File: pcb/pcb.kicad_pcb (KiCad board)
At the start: 6 copper layers, 243.4 x 148.8 mm, 178 parts, among them J1201 Conn_02x07_Top_Bottom, J1401 FPGA_JTAG, J201 USB_B_Mini, J301 Conn_02x07_Odd_Even, J302 1658525-9, J601 DB15_Female_HighDensity, J801 10067847-001RLF, J901 FTSH-110-01-L-DV-007, U1402 S25FL127SABMFV101, U201 TPS54325PWPR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

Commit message: fix new vga
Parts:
- J601: value DB15_Female_HighDensity -> AHDF15A-KG-TAXB; footprint vga:618015330923 -> assvga:AHDF15A-KG-TAXB
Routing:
- net GND: track 239.2 -> 245.0 mm, vias 151 -> 153
- net Net-(J601-Pad14): track 27.9 -> 29.2 mm
- net Net-(J601-Pad13): track 34.1 -> 35.1 mm
- net mcu_debug_reset: track 108.9 -> 109.5 mm
- net Net-(J601-Pad3): track 30.9 -> 31.4 mm

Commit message: logo
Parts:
- added G***: LOGO, raycraft:raycraft, F.Cu at (87.6, 114.8)
- moved J201 16.8 mm to (65.3, 35.4)
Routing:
- net Net-(C216-Pad1): track 56.7 -> 43.8 mm, vias 18 -> 2
- net GND: track 245.0 -> 257.9 mm, vias 153 -> 181
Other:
- board text added: "Carl Aarrestad Ole Peder Brandtzæg Emma Lu Eikemo Sindre Engøy Odd-Erik Frantzen Børge Lundsaunet Sivert Olstad Kasper Midttun Søreide"

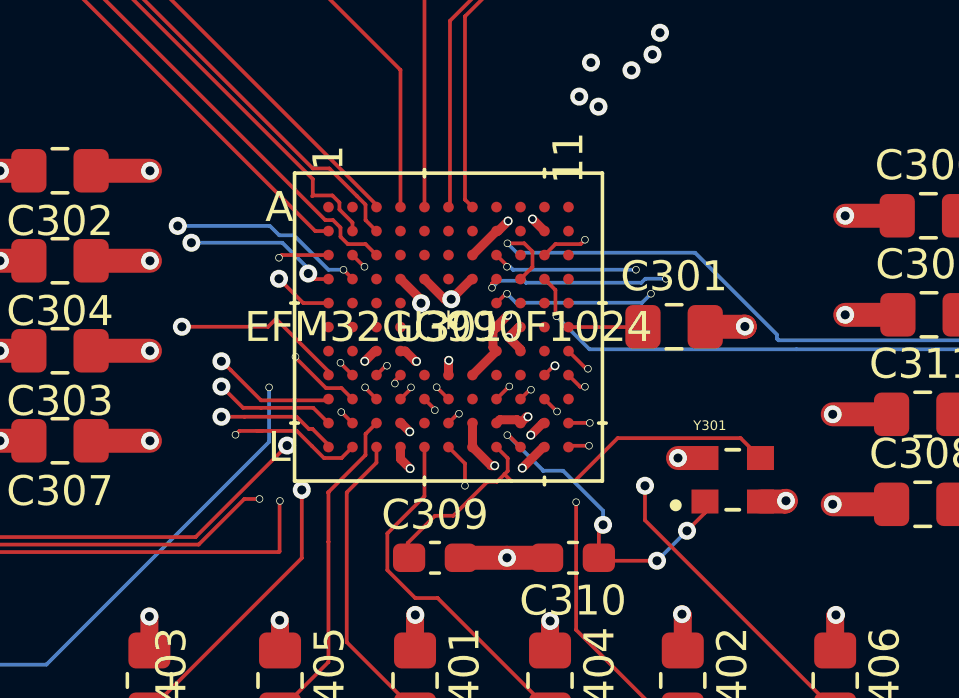
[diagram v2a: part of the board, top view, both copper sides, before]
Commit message: up via size, going to remove onboard-controller
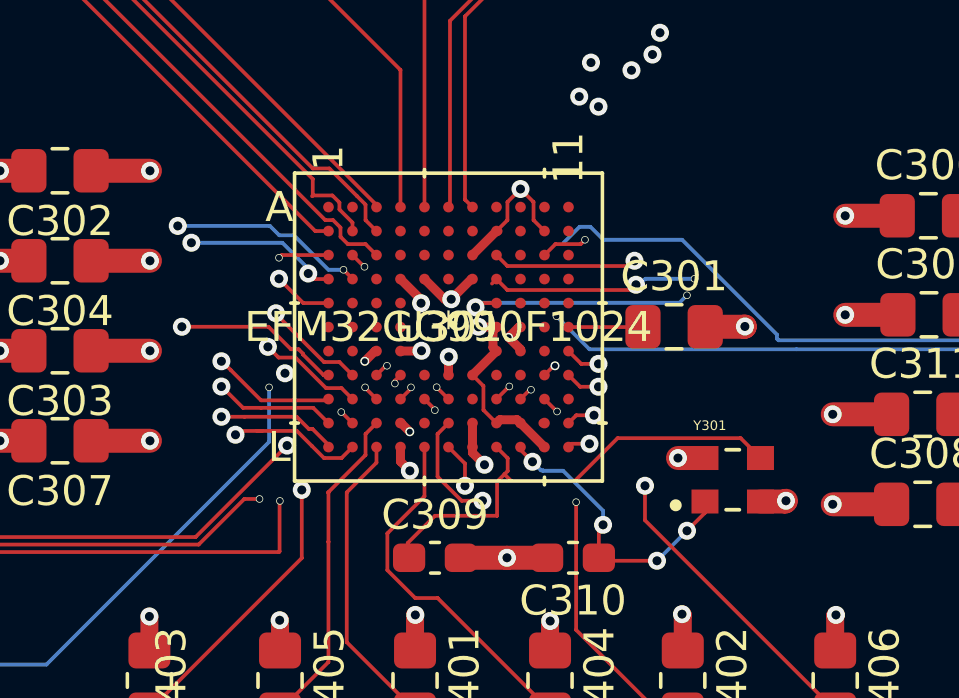
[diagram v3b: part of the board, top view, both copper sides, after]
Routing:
- net mcu_debug_reset: track 109.5 -> 114.0 mm
- net FPGA_PROGRAM_B: track 80.3 -> 76.8 mm, vias 3 -> 2
- net mcu_debug_serial_clock: track 98.9 -> 101.9 mm
- net MCU_DEBUG_US0_MOSI: track 108.4 -> 111.3 mm, vias 1 -> 2
- net MCU_DEBUG_US0_MISO: track 111.2 -> 108.6 mm
- net +3.3V: track 111.6 -> 113.5 mm, vias 79 -> 77
- net GND: track 257.9 -> 259.7 mm, vias 181 -> 179
- net FPGA_DONE: track 84.8 -> 83.4 mm
- net mcu_debug_serial_data: track 96.6 -> 97.8 mm
- net Net-(C310-Pad1): track 11.1 -> 9.93 mm
- net bo_button_2: track 91.9 -> 92.5 mm
- net Net-(C309-Pad1): track 15.3 -> 16.0 mm
- net mcu_debug_serial_out: track 99.9 -> 99.5 mm, vias 3 -> 2

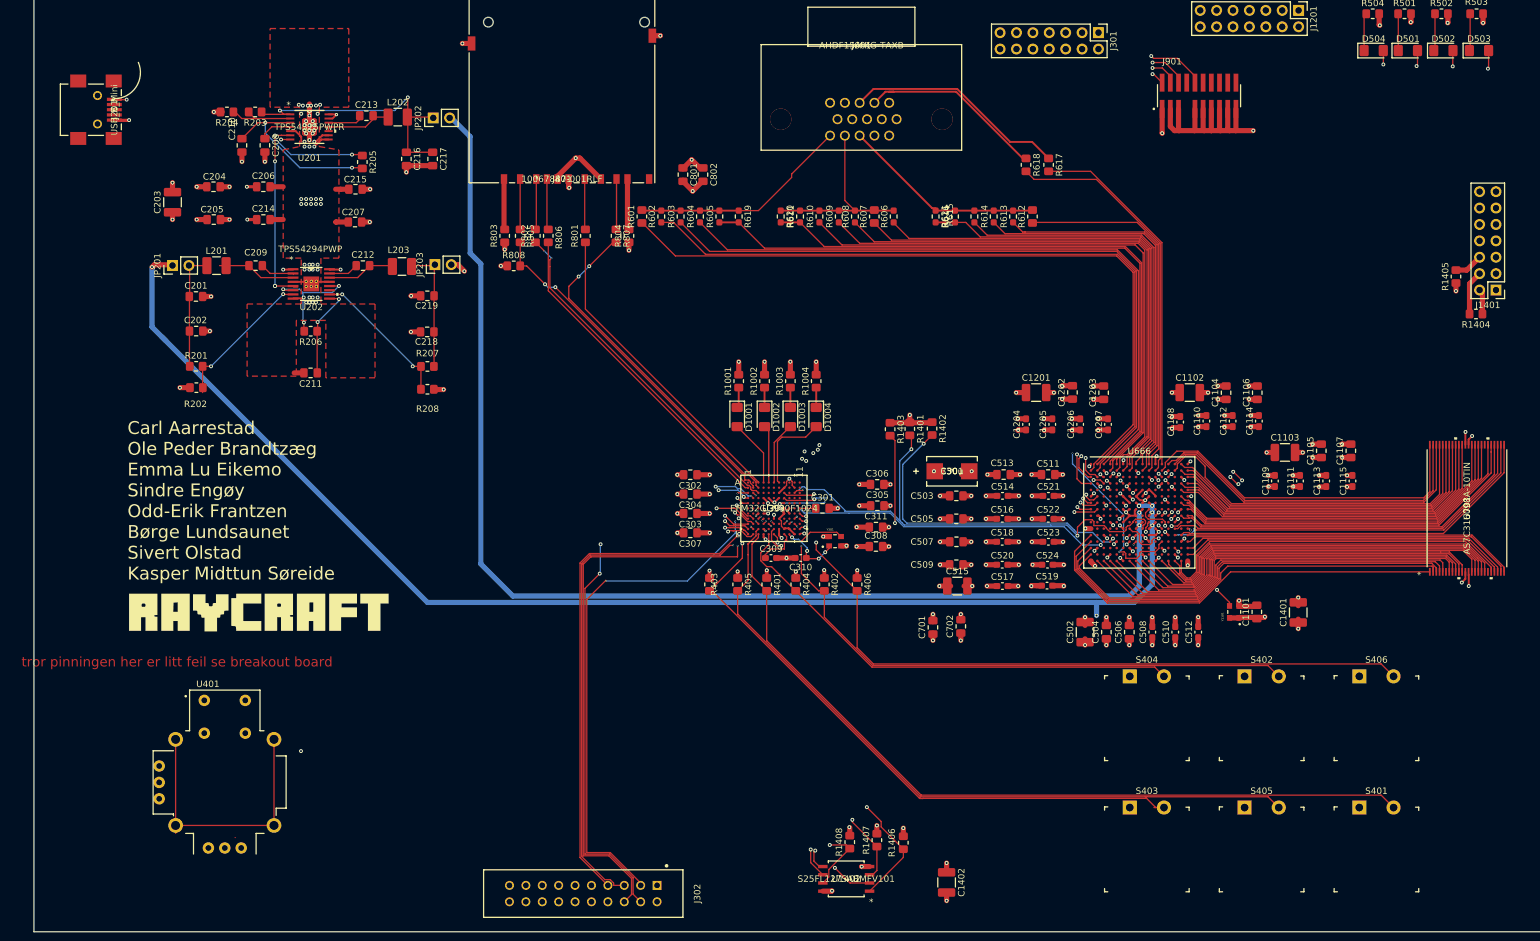
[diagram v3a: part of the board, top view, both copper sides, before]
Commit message: fix vias
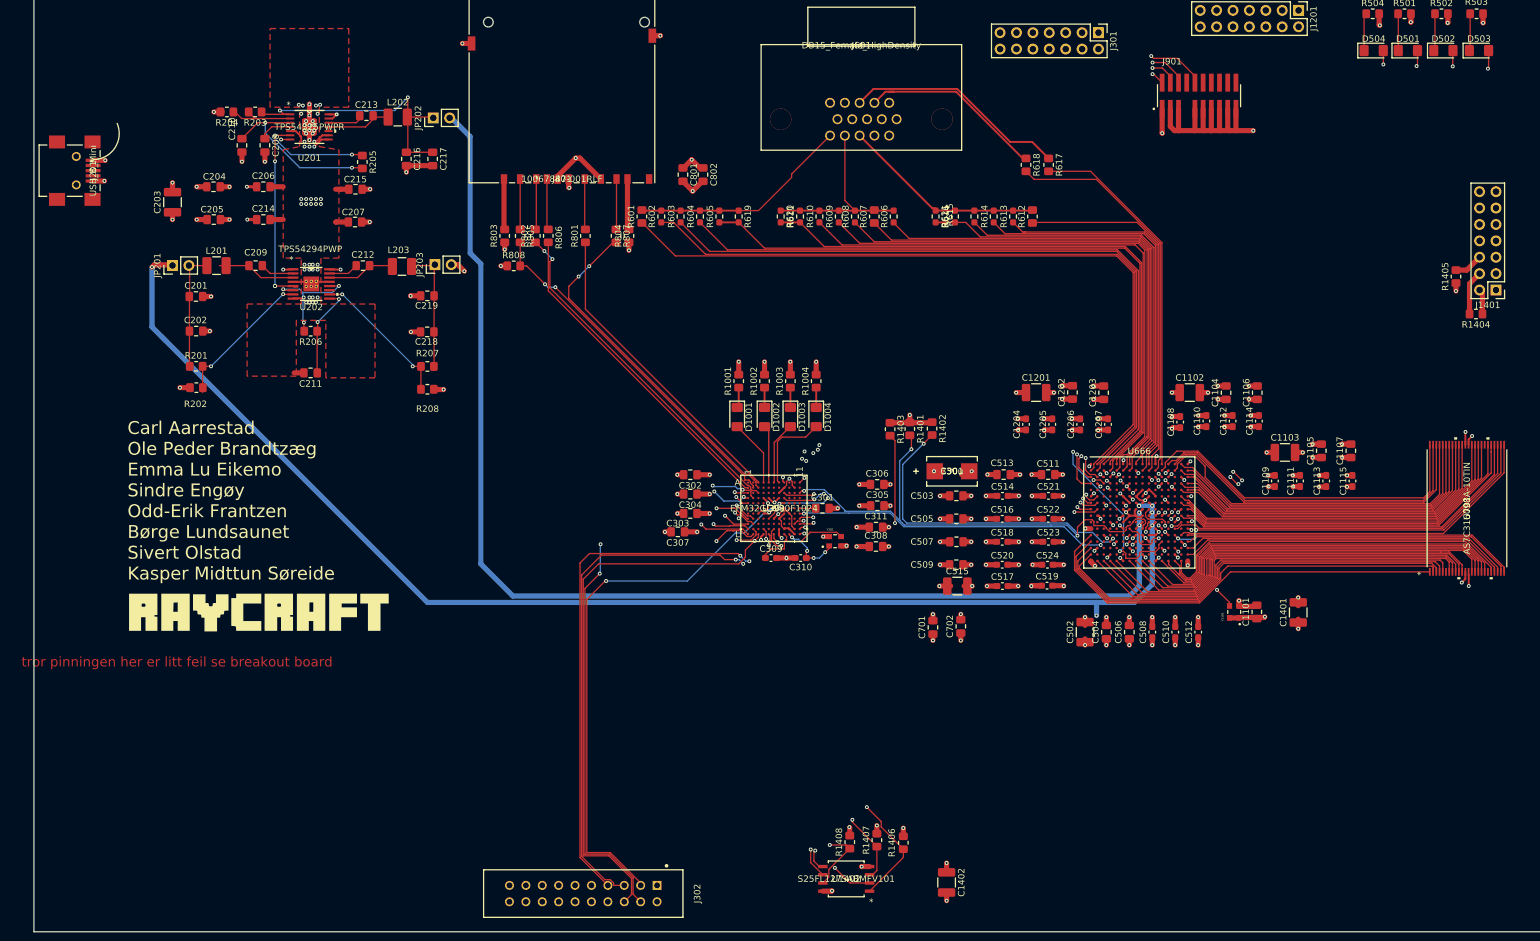
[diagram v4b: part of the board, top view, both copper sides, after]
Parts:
- removed R401, R402, R403, R404, R405, R406: 40k, Resistor_SMD:R_0805_2012Metric_Pad1.20x1.40mm_HandSolder
- removed S401, S402, S403, S404, S405, S406: GPTS203211B, digikey-footprints:PushButton_12x12mm_THT_GPTS203211B
- removed U401: COM-09032, mcu_kicad:XDCR_COM-09032
- J601: value AHDF15A-KG-TAXB -> DB15_Female_HighDensity
- moved J201 9.99 mm to (62.0, 44.8)
- moved C307 1.94 mm to (152.6, 102.3)
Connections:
- J302 pad 5: js_gpio_4 -> js_gpio_4_analog
- J302 pad 7: js_gpio_6 -> js_gpio_6_analog
- R1401 pad 1: +3V3 -> +3.3V
- R1402 pad 1: +3V3 -> +3.3V
- R1403 pad 1: +3V3 -> +3.3V
- U202 pad V: (no net) -> GND
- U301 pad A11: unconnected-(U301-PadA11) -> /Mcu/MCU_GPIO_3
- U301 pad A8: unconnected-(U301-PadA8) -> /Mcu/MCU_GPIO_2
- U301 pad C10: /Mcu/MCU_GPIO_3 -> unconnected-(U301-PadC10)
- U301 pad C11: unconnected-(U301-PadC11) -> FPGA_PROGRAM_B
- U301 pad C2: /Mcu/MCU_GPIO_2 -> unconnected-(U301-PadC2)
- U301 pad D10: FPGA_DONE -> unconnected-(U301-PadD10)
- U301 pad D9: FPGA_PROGRAM_B -> unconnected-(U301-PadD9)
- U301 pad G11: bo_button_6 -> FPGA_DONE
- U301 pad H10: bo_js_vert_1 -> unconnected-(U301-PadH10)
- U301 pad H11: bo_button_2 -> js_gpio_4_analog
- U301 pad H3: js_gpio_5 -> unconnected-(U301-PadH3)
- U301 pad H4: bo_button_3 -> unconnected-(U301-PadH4)
- U301 pad H5: unconnected-(U301-PadH5) -> js_gpio_2
- U301 pad J11: unconnected-(U301-PadJ11) -> js_gpio_6_analog
- U301 pad J3: js_gpio_1 -> unconnected-(U301-PadJ3)
- U301 pad J4: js_gpio_2 -> unconnected-(U301-PadJ4)
- U301 pad J5: js_gpio_3 -> unconnected-(U301-PadJ5)
- U301 pad J6: js_gpio_6 -> unconnected-(U301-PadJ6)
- U301 pad J8: js_gpio_4 -> unconnected-(U301-PadJ8)
- U301 pad J9: bo_js_button_1 -> unconnected-(U301-PadJ9)
- U301 pad K3: bo_button_5 -> unconnected-(U301-PadK3)
- U301 pad L3: bo_button_1 -> js_gpio_3
- U301 pad L5: bo_button_4 -> js_gpio_5
- U301 pad L6: bo_js_hor_1 -> js_gpio_1
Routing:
- net bo_button_1: track 125.7 -> 0.00 mm
- net bo_js_vert_1: track 118.6 -> 0.00 mm, vias 1 -> 0
- net bo_js_button_1: track 112.9 -> 0.00 mm, vias 1 -> 0
- net bo_button_5: track 110.9 -> 0.00 mm
- net bo_button_6: track 109.7 -> 0.00 mm, vias 2 -> 0
- net bo_js_hor_1: track 108.5 -> 0.00 mm, vias 1 -> 0
- net js_gpio_4_analog: track 0.00 -> 104.5 mm, vias 0 -> 3
- net js_gpio_6_analog: track 0.00 -> 102.8 mm, vias 0 -> 3
- net bo_button_3: track 99.3 -> 0.00 mm, vias 2 -> 0
- net bo_button_2: track 92.5 -> 0.00 mm, vias 2 -> 0
- net js_gpio_4: track 89.2 -> 0.00 mm, vias 2 -> 0
- net js_gpio_6: track 84.6 -> 0.00 mm, vias 2 -> 0
- net bo_button_4: track 74.7 -> 0.00 mm
- net unconnected-(U401-PadS1): track 43.1 -> 0.00 mm
- net +3V3: track 7.69 -> 0.00 mm, vias 1 -> 0
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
